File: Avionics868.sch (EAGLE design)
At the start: 69 parts, among them SW1 B3U-1000P-2P-SMD, U1 ATSAMD21G18_QFN, U2 SPX3819M5-L-3-0, U3 MCP73831T-2ACI/OT, U4 MPU-9250, U5 SIM868, U6 BMP280, X1 JSTPH, X2 32.768, X3 ZX62-B-5PA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

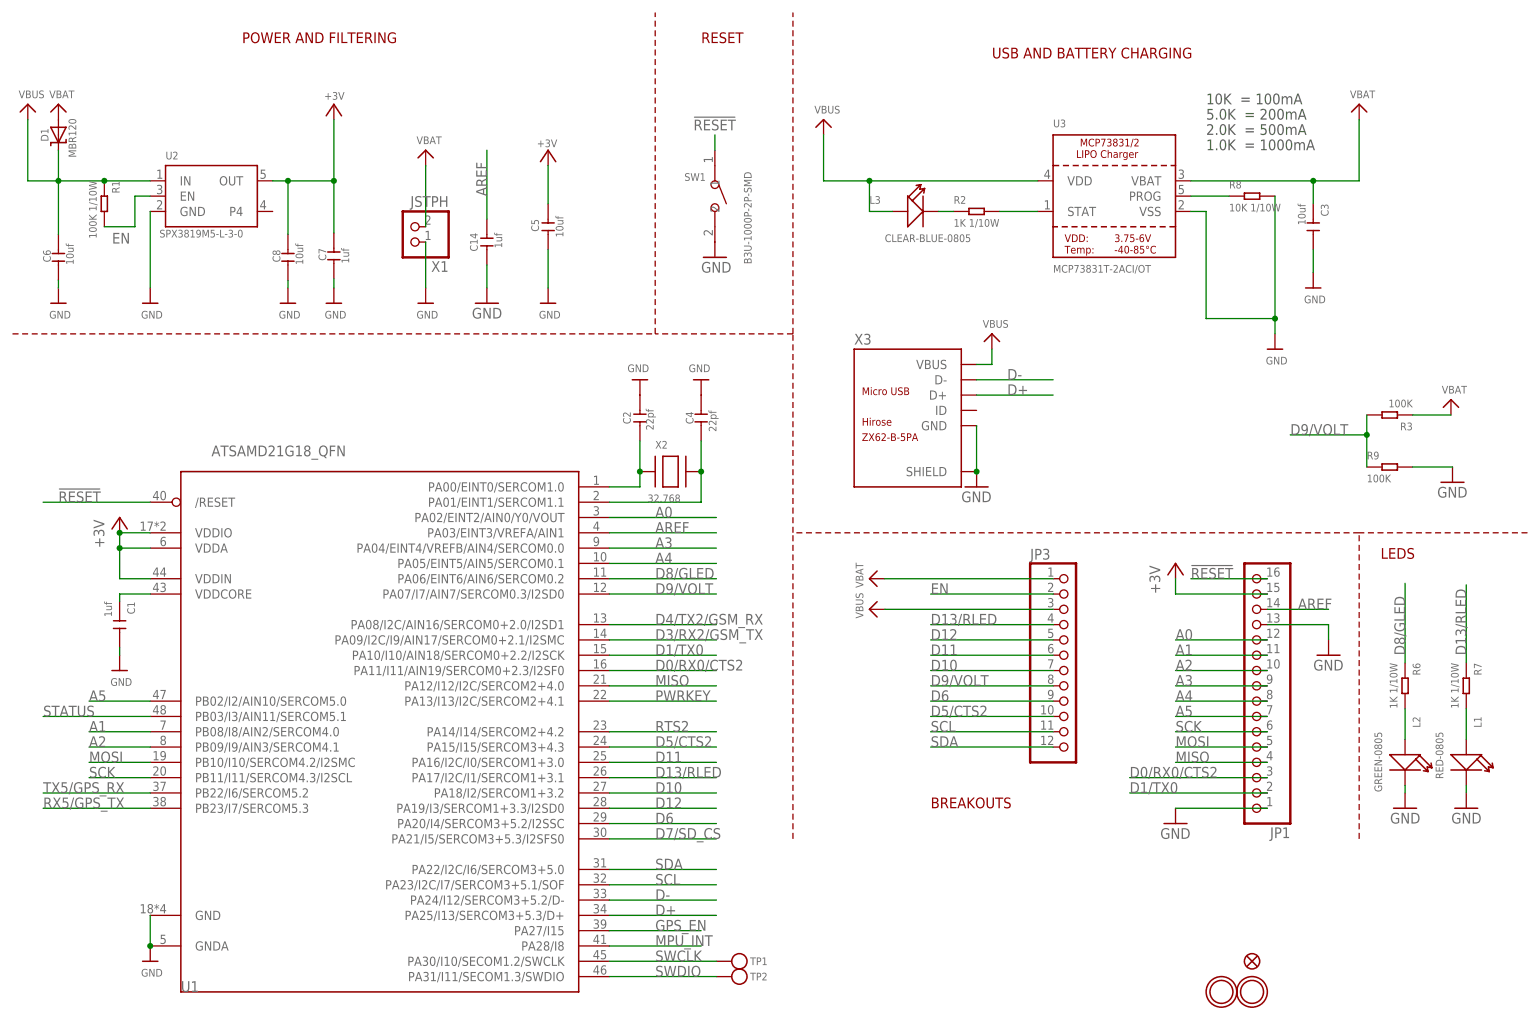
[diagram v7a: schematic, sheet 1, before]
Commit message: removed wattages in resistor values
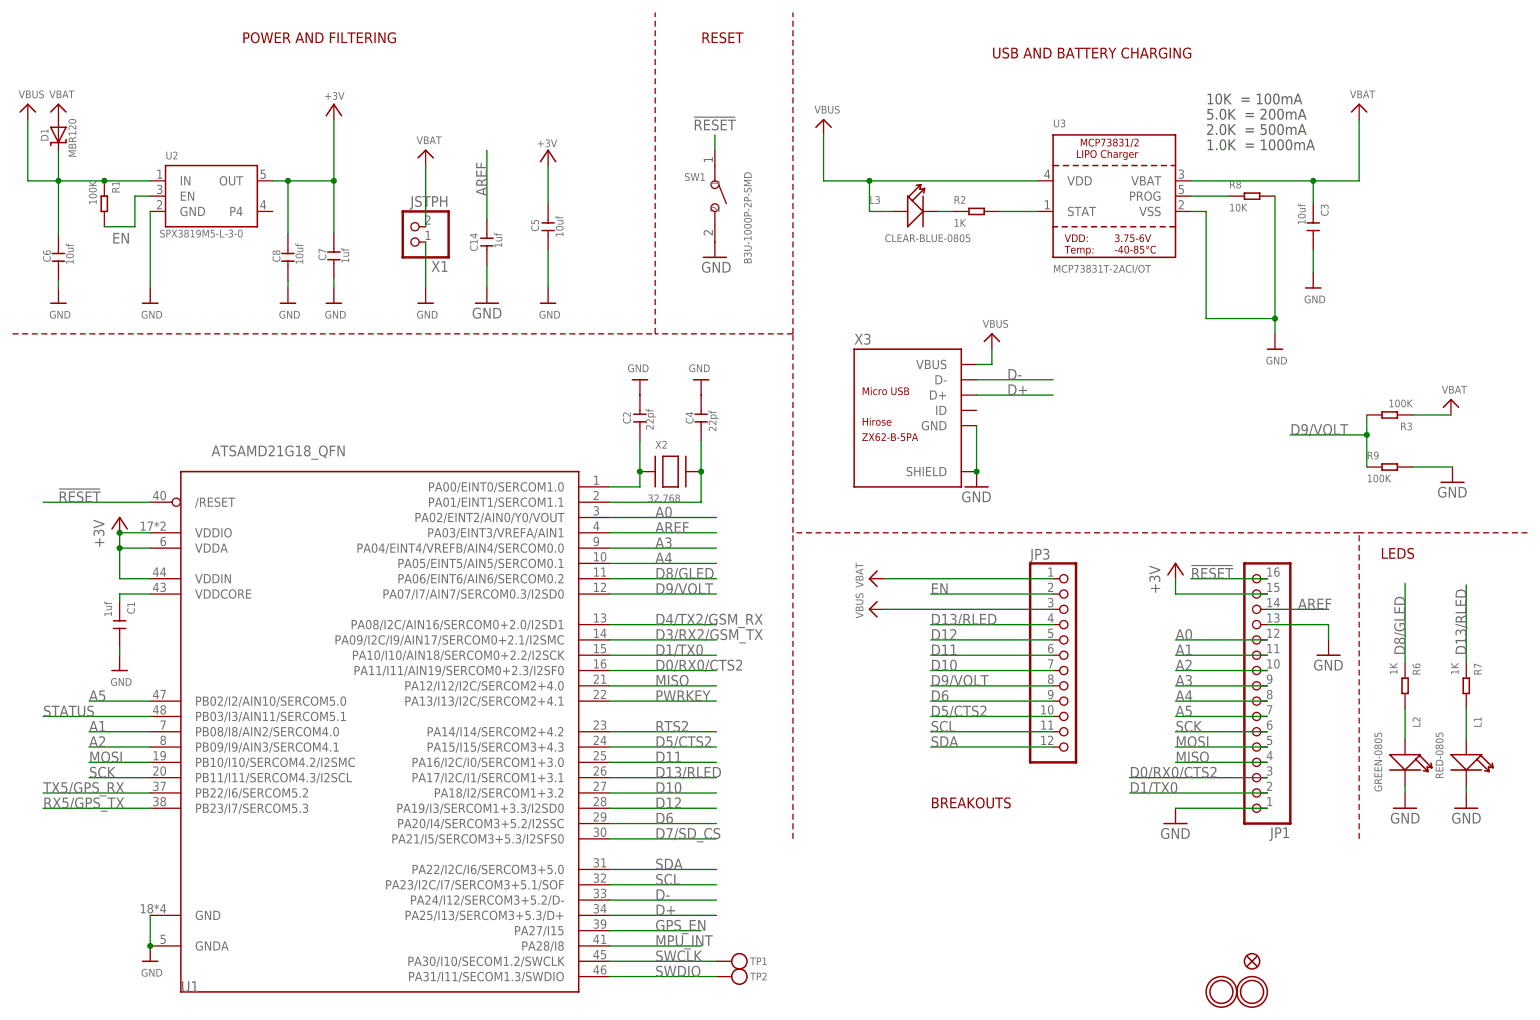
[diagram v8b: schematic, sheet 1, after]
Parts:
- R1: value 100K 1/10W -> 100K
- R2, R6, R7: value 1K 1/10W -> 1K
- R8: value 10K 1/10W -> 10K
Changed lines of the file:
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@@
 <part name="GND7" library="supply1" deviceset="GND" device=""/>
 <part name="C14" library="Seeed-Capacitor-2016" deviceset="CERAMIC-1UF-25V-10%-X7R(0603)" device="" value="1uf"/>
-<part name="R7" library="Seeed-Resistor-2016" deviceset="SMD-RES-1K-5%-1/10W(0603)" device="" value="1K 1/10W"/>
+<part name="R7" library="Seeed-Resistor-2016" deviceset="SMD-RES-1K-5%-1/10W(0603)" device="" value="1K"/>
 <part name="GND10" library="supply1" deviceset="GND" device=""/>
 <part name="U$34" library="microbuilder" deviceset="FIDUCIAL" device="&quot;&quot;"/>
@@
 <part name="U3" library="microbuilder" deviceset="MCP73831/2" device="" value="MCP73831T-2ACI/OT"/>
 <part name="L3" library="Seeed-LED-2016" deviceset="SMD-LED-CLEAR-BLUE(0805)" device="" value="CLEAR-BLUE-0805"/>
-<part name="R2" library="Seeed-Resistor-2016" deviceset="SMD-RES-1K-5%-1/10W(0603)" device="" value="1K 1/10W"/>
+<part name="R2" library="Seeed-Resistor-2016" deviceset="SMD-RES-1K-5%-1/10W(0603)" device="" value="1K"/>
 <part name="C3" library="Seeed-Capacitor-2016" deviceset="CERAMIC-10UF-10V-10%-X5R(0603)" device="" value="10uf"/>
 <part name="U$33" library="microbuilder" deviceset="GND" device=""/>
-<part name="R8" library="Seeed-Resistor-2016" deviceset="SMD-RES-10K-5%-1/10W(0603)" device="" value="10K 1/10W"/>
+<part name="R8" library="Seeed-Resistor-2016" deviceset="SMD-RES-10K-5%-1/10W(0603)" device="" value="10K"/>
 <part name="U$36" library="microbuilder" deviceset="GND" device=""/>
 <part name="U$38" library="microbuilder" deviceset="VBUS" device=""/>
@@
 <part name="TP1" library="microbuilder" deviceset="TESTPOINT" device="ROUND1.5MM"/>
 <part name="TP2" library="microbuilder" deviceset="TESTPOINT" device="ROUND1.5MM"/>
-<part name="R1" library="Seeed-Resistor-2016" deviceset="SMD-RES-100K-5%-1/10W(0603)" device="" value="100K 1/10W"/>
+<part name="R1" library="Seeed-Resistor-2016" deviceset="SMD-RES-100K-5%-1/10W(0603)" device="" value="100K"/>
 <part name="FRAME2" library="microbuilder" deviceset="FRAME_A4" device=""/>
 <part name="U4" library="misc" deviceset="MPU-9250" device=""/>
@@
 <part name="TP5" library="microbuilder" deviceset="TESTPOINT" device="ROUND1.5MM"/>
 <part name="L2" library="Seeed-LED-2016" deviceset="SMD-LED-CLEAR-GREEN(0805)" device="" value="GREEN-0805"/>
-<part name="R6" library="Seeed-Resistor-2016" deviceset="SMD-RES-1K-5%-1/10W(0603)" device="" value="1K 1/10W"/>
+<part name="R6" library="Seeed-Resistor-2016" deviceset="SMD-RES-1K-5%-1/10W(0603)" device="" value="1K"/>
 <part name="GND9" library="supply1" deviceset="GND" device=""/>
 <part name="R3" library="Seeed-Resistor-2016" deviceset="SMD-RES-100K-1%-1/10W(0603)" device="" value="100K"/>
